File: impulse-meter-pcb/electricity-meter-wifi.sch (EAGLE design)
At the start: 10 parts

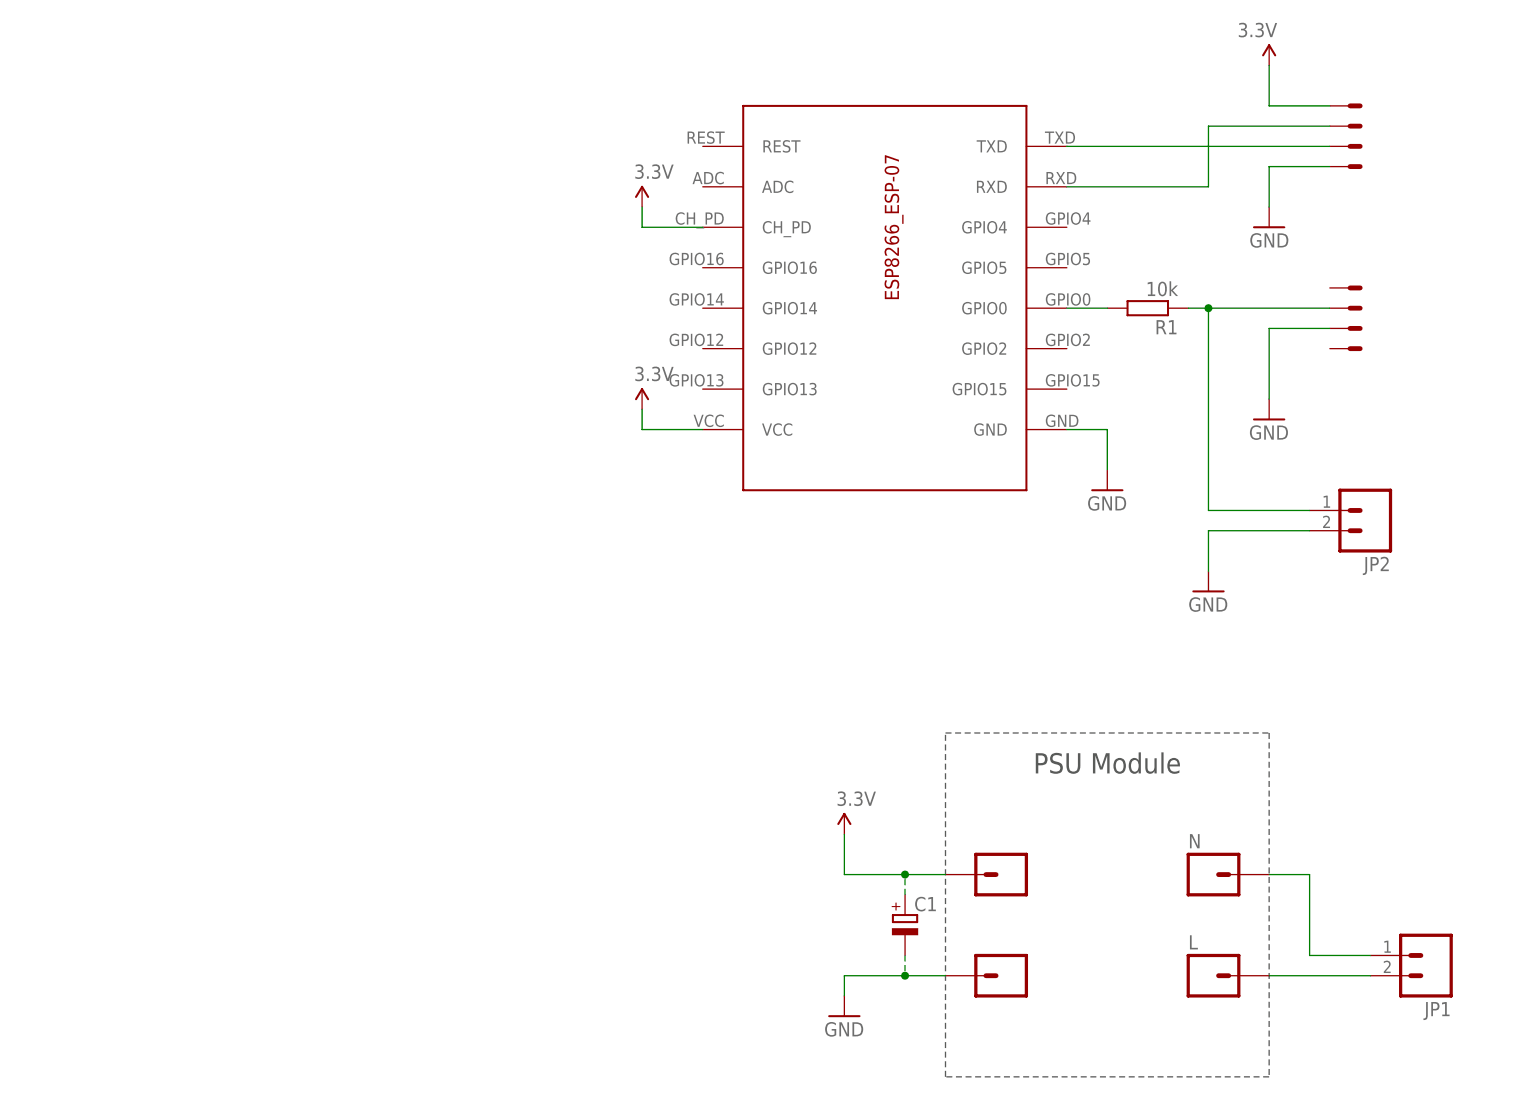
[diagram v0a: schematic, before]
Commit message: pcb: v.1.2.1
moved impulse input to gpio4 and added external pull up
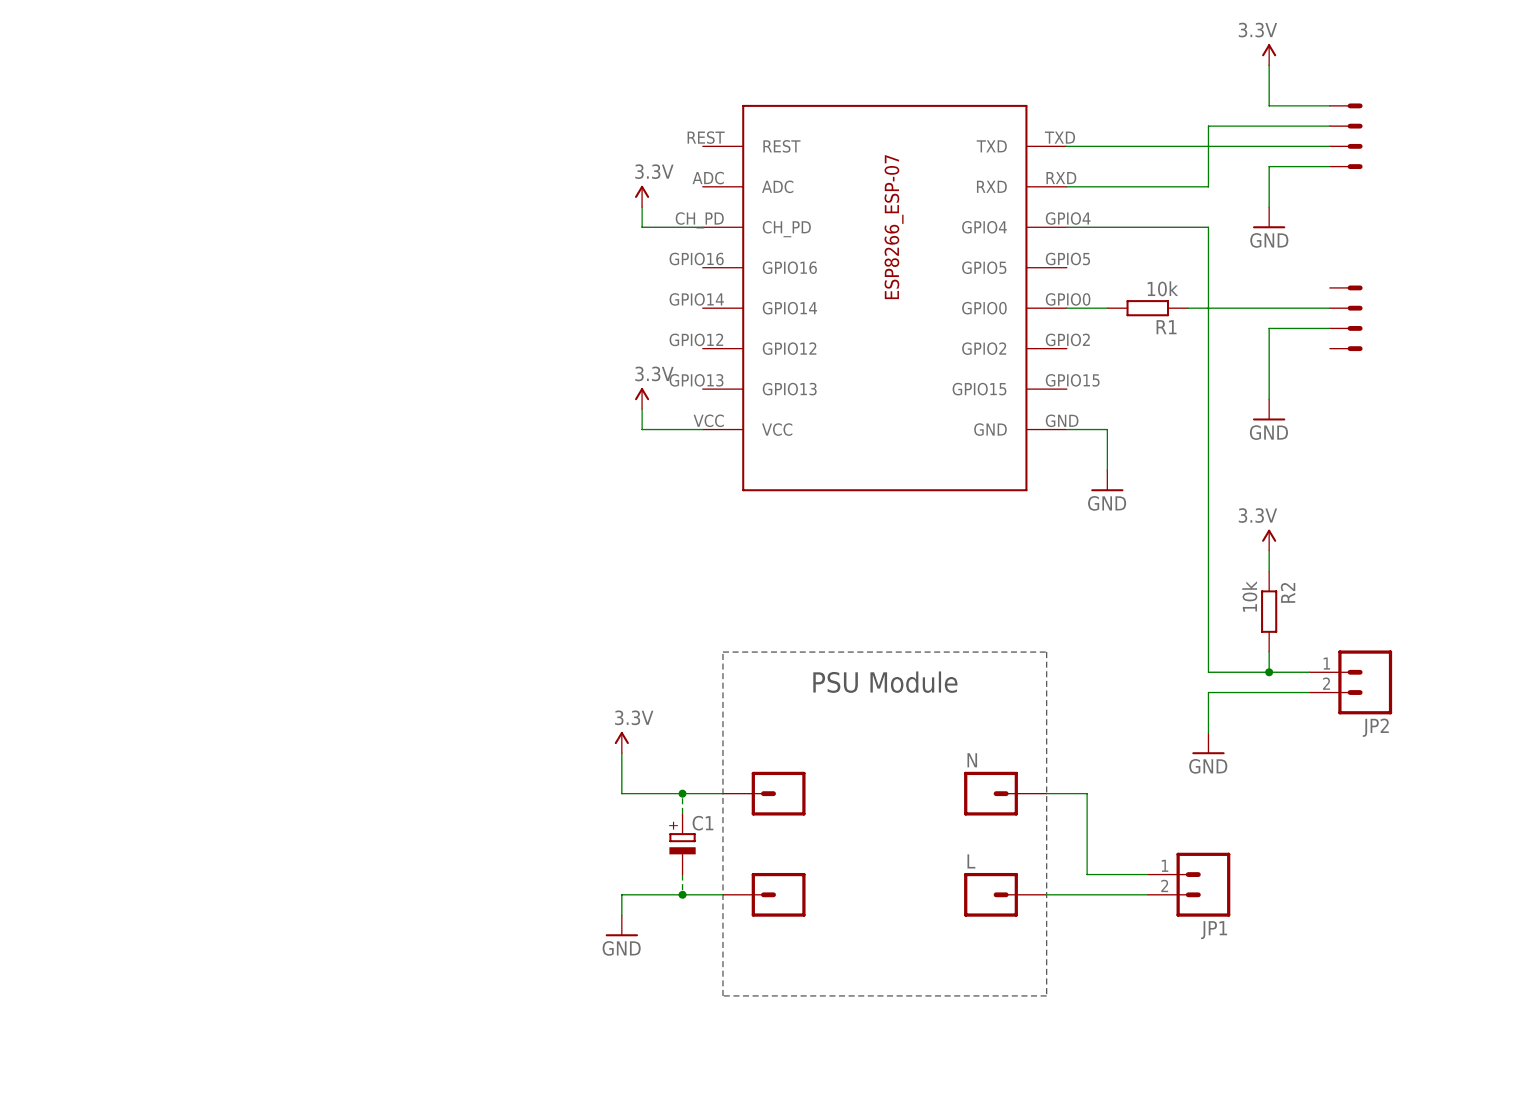
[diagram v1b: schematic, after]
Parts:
- added R2: 10k, rcl:R-EU_R0805
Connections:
- new net N$3: ESP8266_ESP-07.GPIO4, JP2.1, R2.2
- net 3.3V: now also R2.1
- net N$11: no longer JP2.1
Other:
- moved on the sheet: C1, JP1, JP2, L, N
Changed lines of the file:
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@@
 <part name="U$1" library="con-pcb-slot" deviceset="CON-PCB-SLOT-0.05" device="MINIMAL"/>
 <part name="GND2" library="SparkFun-Aesthetics" deviceset="GND" device=""/>
+<part name="R2" library="rcl" deviceset="R-EU_" device="R0805" value="10k"/>
+<part name="SUPPLY3" library="SparkFun-Aesthetics" deviceset="3.3V" device=""/>
 </parts>
 <sheets>
 <sheet>
 <plain>
-<wire x1="116.84" y1="-38.1" x2="116.84" y2="5.08" width="0.1524" layer="97" style="longdash"/>
-<wire x1="116.84" y1="5.08" x2="157.48" y2="5.08" width="0.1524" layer="97" style="longdash"/>
-<wire x1="157.48" y1="5.08" x2="157.48" y2="-38.1" width="0.1524" layer="97" style="longdash"/>
-<wire x1="157.48" y1="-38.1" x2="116.84" y2="-38.1" width="0.1524" layer="97" style="longdash"/>
-<text x="137.16" y="0" size="2.54" layer="97" align="bottom-center">PSU Module</text>
+<wire x1="88.9" y1="-27.94" x2="88.9" y2="15.24" width="0.1524" layer="97" style="longdash"/>
+<wire x1="88.9" y1="15.24" x2="129.54" y2="15.24" width="0.1524" layer="97" style="longdash"/>
+<wire x1="129.54" y1="15.24" x2="129.54" y2="-27.94" width="0.1524" layer="97" style="longdash"/>
+<wire x1="129.54" y1="-27.94" x2="88.9" y2="-27.94" width="0.1524" layer="97" style="longdash"/>
+<text x="109.22" y="10.16" size="2.54" layer="97" align="bottom-center">PSU Module</text>
 </plain>
 <instances>
@@
 <instance part="SUPPLY2" gate="G$1" x="78.74" y="71.12"/>
 <instance part="SUPPLY7" gate="G$1" x="78.74" y="45.72"/>
-<instance part="N" gate="G$1" x="149.86" y="-12.7" smashed="yes">
-<attribute name="NAME" x="147.32" y="-9.398" size="1.778" layer="95"/>
+<instance part="N" gate="G$1" x="121.92" y="-2.54" smashed="yes">
+<attribute name="NAME" x="119.38" y="0.762" size="1.778" layer="95"/>
 </instance>
-<instance part="L" gate="G$1" x="149.86" y="-25.4" smashed="yes">
-<attribute name="NAME" x="147.32" y="-22.098" size="1.778" layer="95"/>
+<instance part="L" gate="G$1" x="121.92" y="-15.24" smashed="yes">
+<attribute name="NAME" x="119.38" y="-11.938" size="1.778" layer="95"/>
 </instance>
-<instance part="3.3V" gate="G$1" x="124.46" y="-12.7" smashed="yes" rot="R180"/>
-<instance part="GND" gate="G$1" x="124.46" y="-25.4" smashed="yes" rot="R180"/>
-<instance part="SUPPLY1" gate="G$1" x="104.14" y="-7.62"/>
-<instance part="GND1" gate="1" x="104.14" y="-30.48"/>
-<instance part="JP1" gate="G$1" x="177.8" y="-22.86" rot="R180"/>
-<instance part="JP2" gate="G$1" x="170.18" y="33.02" rot="R180"/>
-<instance part="C1" gate="G$1" x="111.76" y="-17.78"/>
+<instance part="3.3V" gate="G$1" x="96.52" y="-2.54" smashed="yes" rot="R180"/>
+<instance part="GND" gate="G$1" x="96.52" y="-15.24" smashed="yes" rot="R180"/>
+<instance part="SUPPLY1" gate="G$1" x="76.2" y="2.54"/>
+<instance part="GND1" gate="1" x="76.2" y="-20.32"/>
+<instance part="JP1" gate="G$1" x="149.86" y="-12.7" rot="R180"/>
+<instance part="JP2" gate="G$1" x="170.18" y="12.7" rot="R180"/>
+<instance part="C1" gate="G$1" x="83.82" y="-7.62"/>
 <instance part="U$1" gate="G$1" x="165.1" y="76.2" smashed="yes" rot="MR180"/>
 <instance part="U$1" gate="G$2" x="165.1" y="78.74" smashed="yes" rot="MR180"/>
 <instance part="U$1" gate="G$3" x="165.1" y="81.28" smashed="yes" rot="MR180"/>
 <instance part="U$1" gate="G$4" x="165.1" y="83.82" smashed="yes" rot="MR180"/>
-<instance part="GND2" gate="1" x="149.86" y="22.86"/>
+<instance part="GND2" gate="1" x="149.86" y="2.54"/>
 <instance part="U$1" gate="G$5" x="165.1" y="60.96" smashed="yes"/>
 <instance part="U$1" gate="G$6" x="165.1" y="58.42" smashed="yes"/>
 <instance part="U$1" gate="G$7" x="165.1" y="55.88" smashed="yes"/>
 <instance part="U$1" gate="G$8" x="165.1" y="53.34" smashed="yes"/>
+<instance part="R2" gate="G$1" x="157.48" y="20.32" rot="R270"/>
+<instance part="SUPPLY3" gate="G$1" x="157.48" y="27.94" rot="MR0"/>
 </instances>
 <busses>
@@
 <pinref part="GND" gate="G$1" pin="1"/>
 <pinref part="GND1" gate="1" pin="GND"/>
-<wire x1="116.84" y1="-25.4" x2="111.76" y2="-25.4" width="0.1524" layer="91"/>
-<wire x1="111.76" y1="-25.4" x2="104.14" y2="-25.4" width="0.1524" layer="91"/>
-<wire x1="104.14" y1="-25.4" x2="104.14" y2="-27.94" width="0.1524" layer="91"/>
+<wire x1="88.9" y1="-15.24" x2="83.82" y2="-15.24" width="0.1524" layer="91"/>
+<wire x1="83.82" y1="-15.24" x2="76.2" y2="-15.24" width="0.1524" layer="91"/>
+<wire x1="76.2" y1="-15.24" x2="76.2" y2="-17.78" width="0.1524" layer="91"/>
 <pinref part="C1" gate="G$1" pin="-"/>
-<wire x1="111.76" y1="-22.86" x2="111.76" y2="-25.4" width="0.1524" layer="91" style="longdash"/>
-<junction x="111.76" y="-25.4"/>
+<wire x1="83.82" y1="-12.7" x2="83.82" y2="-15.24" width="0.1524" layer="91" style="longdash"/>
+<junction x="83.82" y="-15.24"/>
 </segment>
 <segment>
 <pinref part="GND2" gate="1" pin="GND"/>
-<wire x1="149.86" y1="30.48" x2="149.86" y2="25.4" width="0.1524" layer="91"/>
+<wire x1="149.86" y1="10.16" x2="149.86" y2="5.08" width="0.1524" layer="91"/>
 <pinref part="JP2" gate="G$1" pin="2"/>
-<wire x1="149.86" y1="30.48" x2="162.56" y2="30.48" width="0.1524" layer="91"/>
+<wire x1="149.86" y1="10.16" x2="162.56" y2="10.16" width="0.1524" layer="91"/>
 </segment>
 <segment>
@@
 <pinref part="3.3V" gate="G$1" pin="1"/>
 <pinref part="SUPPLY1" gate="G$1" pin="3.3V"/>
-<wire x1="116.84" y1="-12.7" x2="111.76" y2="-12.7" width="0.1524" layer="91"/>
-<wire x1="111.76" y1="-12.7" x2="104.14" y2="-12.7" width="0.1524" layer="91"/>
-<wire x1="104.14" y1="-12.7" x2="104.14" y2="-7.62" width="0.1524" layer="91"/>
+<wire x1="88.9" y1="-2.54" x2="83.82" y2="-2.54" width="0.1524" layer="91"/>
+<wire x1="83.82" y1="-2.54" x2="76.2" y2="-2.54" width="0.1524" layer="91"/>
+<wire x1="76.2" y1="-2.54" x2="76.2" y2="2.54" width="0.1524" layer="91"/>
 <pinref part="C1" gate="G$1" pin="+"/>
-<wire x1="111.76" y1="-15.24" x2="111.76" y2="-12.7" width="0.1524" layer="91" style="longdash"/>
-<junction x="111.76" y="-12.7"/>
+<wire x1="83.82" y1="-5.08" x2="83.82" y2="-2.54" width="0.1524" layer="91" style="longdash"/>
+<junction x="83.82" y="-2.54"/>
 </segment>
 <segment>
@@
 <wire x1="157.48" y1="83.82" x2="157.48" y2="88.9" width="0.1524" layer="91"/>
 </segment>
+<segment>
+<pinref part="R2" gate="G$1" pin="1"/>
+<pinref part="SUPPLY3" gate="G$1" pin="3.3V"/>
+<wire x1="157.48" y1="25.4" x2="157.48" y2="27.94" width="0.1524" layer="91"/>
+</segment>
 </net>
 <net name="N$11" class="0">
 <segment>
-<pinref part="JP2" gate="G$1" pin="1"/>
-<wire x1="162.56" y1="33.02" x2="149.86" y2="33.02" width="0.1524" layer="91"/>
 <pinref part="R1" gate="G$1" pin="1"/>
-<wire x1="147.32" y1="58.42" x2="149.86" y2="58.42" width="0.1524" layer="91"/>
-<wire x1="149.86" y1="33.02" x2="149.86" y2="58.42" width="0.1524" layer="91"/>
 <pinref part="U$1" gate="G$6" pin="S"/>
-<wire x1="149.86" y1="58.42" x2="165.1" y2="58.42" width="0.1524" layer="91"/>
-<junction x="149.86" y="58.42"/>
+<wire x1="147.32" y1="58.42" x2="165.1" y2="58.42" width="0.1524" layer="91"/>
 </segment>
 </net>
@@
 <pinref part="JP1" gate="G$1" pin="2"/>
 <pinref part="L" gate="G$1" pin="1"/>
-<wire x1="170.18" y1="-25.4" x2="157.48" y2="-25.4" width="0.1524" layer="91"/>
+<wire x1="142.24" y1="-15.24" x2="129.54" y2="-15.24" width="0.1524" layer="91"/>
 </segment>
 </net>
@@
 <segment>
 <pinref part="JP1" gate="G$1" pin="1"/>
-<wire x1="170.18" y1="-22.86" x2="162.56" y2="-22.86" width="0.1524" layer="91"/>
-<wire x1="162.56" y1="-22.86" x2="162.56" y2="-12.7" width="0.1524" layer="91"/>
+<wire x1="142.24" y1="-12.7" x2="134.62" y2="-12.7" width="0.1524" layer="91"/>
+<wire x1="134.62" y1="-12.7" x2="134.62" y2="-2.54" width="0.1524" layer="91"/>
 <pinref part="N" gate="G$1" pin="1"/>
-<wire x1="162.56" y1="-12.7" x2="157.48" y2="-12.7" width="0.1524" layer="91"/>
+<wire x1="134.62" y1="-2.54" x2="129.54" y2="-2.54" width="0.1524" layer="91"/>
 </segment>
 </net>
@@
 </segment>
 </net>
+<net name="N$3" class="0">
+<segment>
+<pinref part="JP2" gate="G$1" pin="1"/>
+<wire x1="162.56" y1="12.7" x2="157.48" y2="12.7" width="0.1524" layer="91"/>
+<pinref part="R2" gate="G$1" pin="2"/>
+<wire x1="157.48" y1="15.24" x2="157.48" y2="12.7" width="0.1524" layer="91"/>
+<junction x="157.48" y="12.7"/>
+<wire x1="157.48" y1="12.7" x2="149.86" y2="12.7" width="0.1524" layer="91"/>
+<pinref part="ESP8266_ESP-07" gate="G$1" pin="GPIO4"/>
+<wire x1="132.08" y1="68.58" x2="149.86" y2="68.58" width="0.1524" layer="91"/>
+<wire x1="149.86" y1="68.58" x2="149.86" y2="12.7" width="0.1524" layer="91"/>
+</segment>
+</net>
